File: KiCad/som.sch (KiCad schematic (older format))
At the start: 38 parts, among them T2 BSS138APW, T4 BSS138APW, T5 BSS138APW

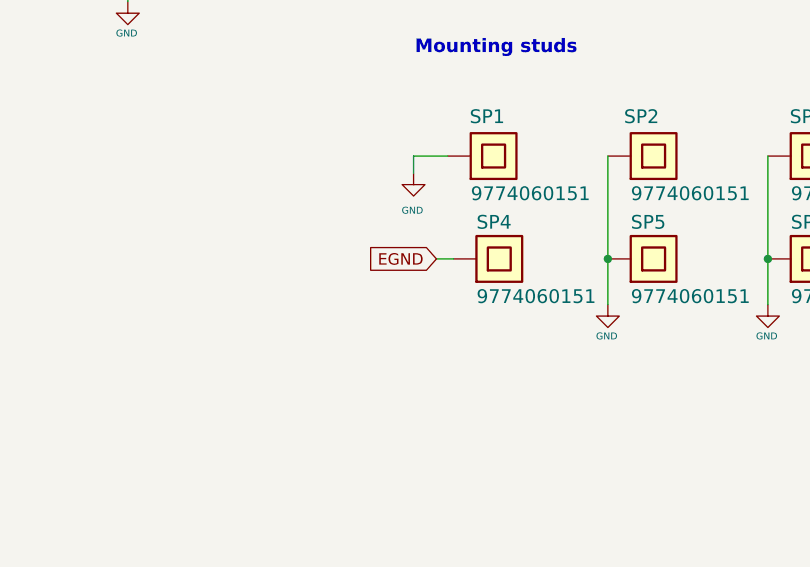
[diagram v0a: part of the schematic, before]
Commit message: Connect spacer to GND
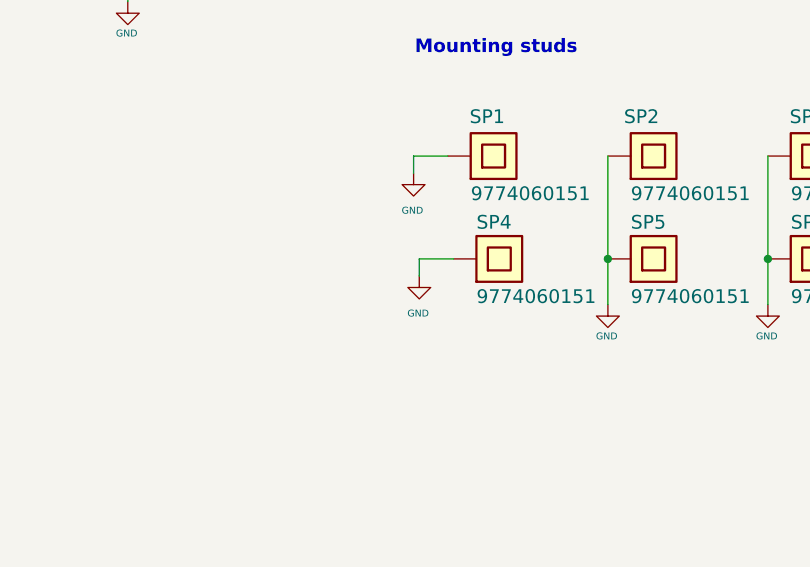
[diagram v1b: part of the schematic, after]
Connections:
- net labels removed: EGND
- wire segments 308 -> 309
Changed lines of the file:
@@
 Text GLabel 14125 2050 0    50   Input ~ 0
 5V0_SYS
-Text GLabel 13650 9225 0    50   Input ~ 0
-EGND
 Text Notes 500  750  0    118  ~ 24
 SoM
@@
 Wire Wire Line
 	13775 2600 14275 2600
-Wire Wire Line
-	13650 9225 13725 9225
 $Comp
 L jetson-nano-baseboard:GND #GND_052
@@
 Text GLabel 6450 3350 0    50   Input ~ 0
 SPI0_SCK
+$Comp
+L jetson-nano-baseboard:GND #GND_?
+U 1 1 623364F3
+P 13575 9300
+F 0 "#GND_?" H 13575 9300 20  0001 C CNN
+F 1 "GND" H 13570 9137 30  0000 C CNN
+F 2 "" H 13575 9300 70  0001 C CNN
+F 3 "" H 13575 9300 70  0001 C CNN
+	1    13575 9300
+	1    0    0    -1
+$EndComp
+Wire Wire Line
+	13725 9225 13575 9225
+Wire Wire Line
+	13575 9225 13575 9300
 $EndSCHEMATC
